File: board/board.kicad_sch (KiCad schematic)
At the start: 23 parts, among them J1 port attiny, J10 BMS Bat +, J11 BMS Bat gnd, J12 BMS out -, J13 BMS in +5v, J14 BMS in gnd, J15 alim mp3 -, J17 next, J18 vol -, J2 Conn_01x02_Pin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

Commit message: ajout etiquette global + plan de masse
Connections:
- net Next + mp3: now reaches J1.1 (Pin_1), J17.1 (Pin_1)
- net vol - mp3: now reaches J1.3 (Pin_3), J18.1 (Pin_1)
- net bouton NEXT: now reaches J1.4 (Pin_4), J24.10 (Pin_10), R1.2
- net bouton VOL -: now reaches J1.5 (Pin_5), J24.9 (Pin_9), R2.2
- net bat gnd: now reaches F1.2, J24.2 (Pin_2)
- net bat +: now reaches J11.1 (Pin_1), J24.1 (Pin_1)
- net BMS out -: now reaches J12.1 (Pin_1), J8.1 (Pin_1)
- net BMS in +: now reaches J13.1 (Pin_1), J24.3 (Pin_3)
- net BMS in gnd: now reaches J14.1 (Pin_1), J24.4 (Pin_4)
- net on/off out: now reaches J24.5 (Pin_5), J7.1 (Pin_1)
- net on/off in: now reaches J24.6 (Pin_6), J9.1 (Pin_1)
- net HP +: now reaches J24.7 (Pin_7), J4.1 (Pin_1)
- net HP -: now reaches J24.8 (Pin_8), J4.2 (Pin_2)
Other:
- note added: "Commande mp3"
- note added: "Connecteur JST GH TBT (vertical)"
- moved on the sheet: F1, J10, J13, J14, J17, J18, J24, J4, J7, J8, J9, R1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

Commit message: ajout empreinte STM8 + CH32V0003
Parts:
- added U1: ATtiny85-20S, Package_SO:SOIC-8_5.3x5.3mm_P1.27mm, symbol MCU_Microchip_ATtiny:ATtiny85-20S
- added U2: ATtiny85V-10P, Package_DIP:DIP-8_W7.62mm, symbol MCU_Microchip_ATtiny:ATtiny85V-10P
- added U3: STM8S001J3M, Package_SO:SO-8_3.9x4.9mm_P1.27mm, symbol MCU_ST_STM8:STM8S001J3M
- added U4: CH32V003AxMx, Package_SO:SOP-16_3.9x9.9mm_P1.27mm, symbol MCU_WCH_CH32V0:CH32V003AxMx
- J1: footprint Connector_PinHeader_2.54mm:PinHeader_1x06_P2.54mm_Vertical -> Connector_PinSocket_2.54mm:PinSocket_1x06_P2.54mm_Vertical
- J2: footprint Connector_PinHeader_2.54mm:PinHeader_1x02_P2.54mm_Vertical -> Connector_PinSocket_2.54mm:PinSocket_1x02_P2.54mm_Vertical
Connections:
- net GND: now also U1.4 (GND), U2.4 (GND), U3.2 (VSS), U4.14 (VSS)
- net Next + mp3: now also U1.5 (AREF/PB0), U2.5 (AREF/PB0), U3.1 (PD6), U4.3 (PC3)
- net VCC: now also U1.8 (VCC), U2.8 (VCC), U3.4 (VDD), U4.15 (VDD)
- net bouton NEXT: now also U1.2 (XTAL1/PB3), U2.2 (XTAL1/PB3), U3.5 (PB5), U4.1 (PC1)
- net bouton VOL -: now also U1.3 (XTAL2/PB4), U2.3 (XTAL2/PB4), U3.6 (PB4), U4.2 (PC2)
- net vol - mp3: now also U1.7 (PB2), U2.7 (PB2), U3.7 (PC5), U4.4 (PC4)
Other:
- note added: "CH32V003AxMx"
- note added: "STM8S001J3"
- note added: "TINY SOP8"
- note added: "Tiny DIP8"
- moved on the sheet: C3, C4, F1, J1, J10, J13, J14, J15, J17, J18, J2, J24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

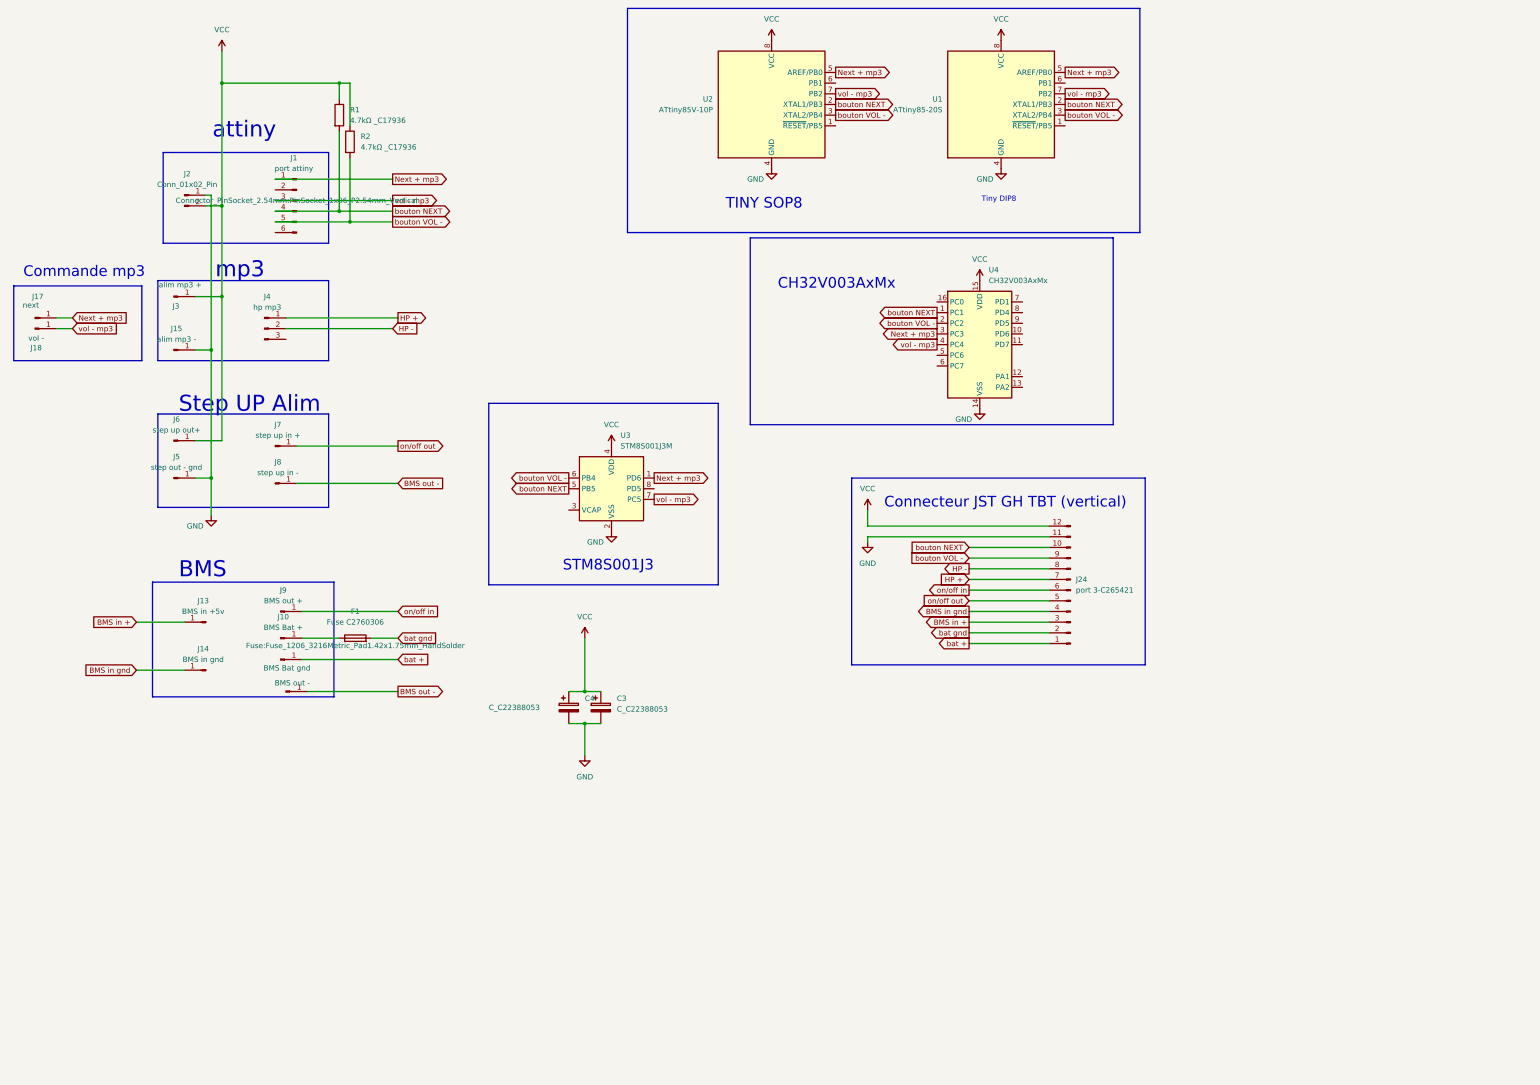
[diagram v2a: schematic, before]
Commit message: mise a jour marquage pcb et ajout programation tiny dans le source, ajout autre famille ucontrolleur STM8 et wch
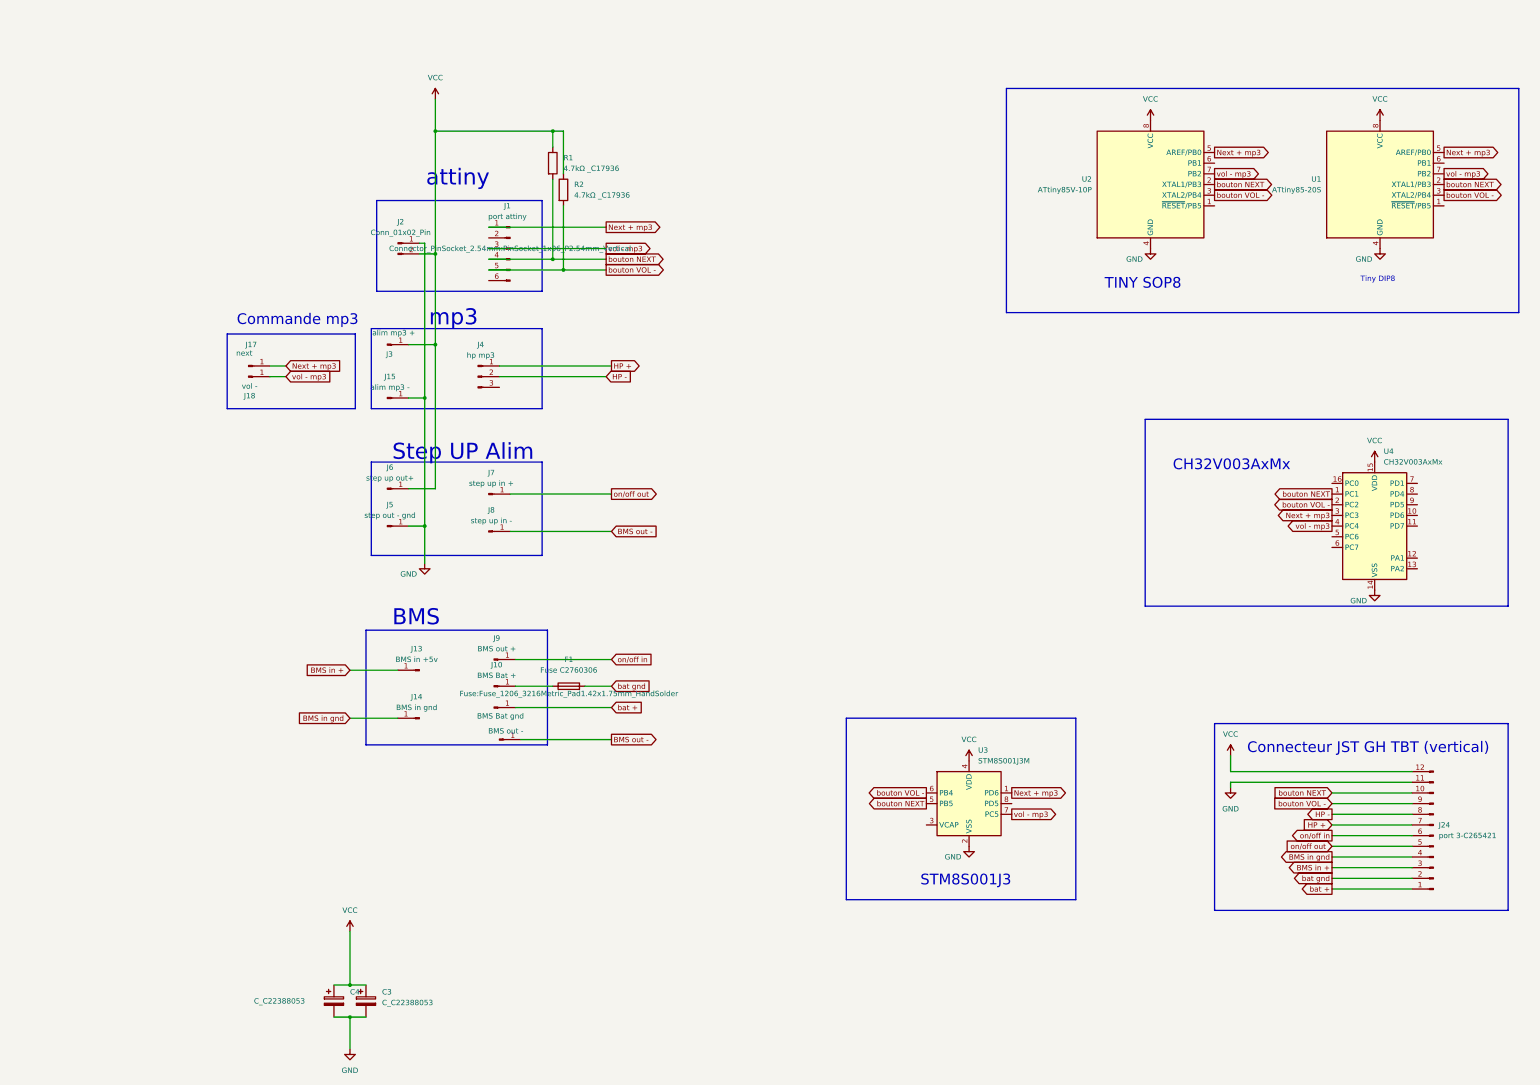
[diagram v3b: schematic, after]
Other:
- moved on the sheet: C3, C4, F1, J1, J10, J13, J14, J15, J17, J18, J2, J24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
